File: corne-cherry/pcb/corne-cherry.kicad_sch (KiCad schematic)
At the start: 122 parts, among them J1 MJ-4PP-9, J2 OLED, J3 LED, P1 i2c-pin, P2 i2c-pin, SW1 SW_PUSH, SW10 SW_PUSH, SW11 SW_PUSH, SW12 SW_PUSH, SW13 SW_PUSH, SW14 SW_PUSH, SW15 SW_PUSH, SW16 SW_PUSH, SW17 SW_PUSH, SW18 SW_PUSH, SW19 SW_PUSH, SW2 SW_PUSH, SW20 SW_PUSH, SW21 SW_PUSH, SW22 SW_PUSH, SW23 SW_PUSH, SW24 SW_PUSH, SW25 SW_PUSH, SW26 SW_PUSH, SW3 SW_PUSH, SW4 SW_PUSH, SW5 SW_PUSH, SW6 SW_PUSH, SW7 SW_PUSH, SW8 SW_PUSH, SW9 SW_PUSH, U1 ProMicro, U3 D, U5 D

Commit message: v.1.0
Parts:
- removed H3, H4: MountingHole, EKR82-footprint:HOLE_M3-3.2-3.5, symbol Mechanical:MountingHole
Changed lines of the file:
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@@
-    )
-  )
-  (symbol (lib_id "Mechanical:MountingHole") (at 313.055 66.04 0) (unit 1)
-    (in_bom yes) (on_board yes)
-    (property "Reference" "H3" (id 0) (at 315.595 64.8716 0)
-      (effects (font (size 1.27 1.27)) (justify left))
-    )
-    (property "Value" "MountingHole" (id 1) (at 315.595 67.183 0)
-      (effects (font (size 1.27 1.27)) (justify left))
-    )
-    (property "Footprint" "EKR82-footprint:HOLE_M3-3.2-3.5" (id 2) (at 313.055 66.04 0)
-      (effects (font (size 1.27 1.27)) hide)
-    )
-    (property "Datasheet" "~" (id 3) (at 313.055 66.04 0)
-      (effects (font (size 1.27 1.27)) hide)
-    )
-  )
-  (symbol (lib_id "Mechanical:MountingHole") (at 313.055 70.485 0) (unit 1)
-    (in_bom yes) (on_board yes)
-    (property "Reference" "H4" (id 0) (at 315.595 69.3166 0)
-      (effects (font (size 1.27 1.27)) (justify left))
-    )
-    (property "Value" "MountingHole" (id 1) (at 315.595 71.628 0)
-      (effects (font (size 1.27 1.27)) (justify left))
-    )
-    (property "Footprint" "EKR82-footprint:HOLE_M3-3.2-3.5" (id 2) (at 313.055 70.485 0)
-      (effects (font (size 1.27 1.27)) hide)
-    )
-    (property "Datasheet" "~" (id 3) (at 313.055 70.485 0)
-      (effects (font (size 1.27 1.27)) hide)
     )
   )
@@
       (reference "H2") (unit 1) (value "MountingHole") (footprint "EKR82-footprint:HOLE_M3-3.2-3.5")
     )
-    (path "/00000000-0000-0000-0000-00005d323d8e"
-      (reference "H3") (unit 1) (value "MountingHole") (footprint "EKR82-footprint:HOLE_M3-3.2-3.5")
-    )
-    (path "/00000000-0000-0000-0000-00005d3381c5"
-      (reference "H4") (unit 1) (value "MountingHole") (footprint "EKR82-footprint:HOLE_M3-3.2-3.5")
-    )
     (path "/00000000-0000-0000-0000-00005d34c5d1"

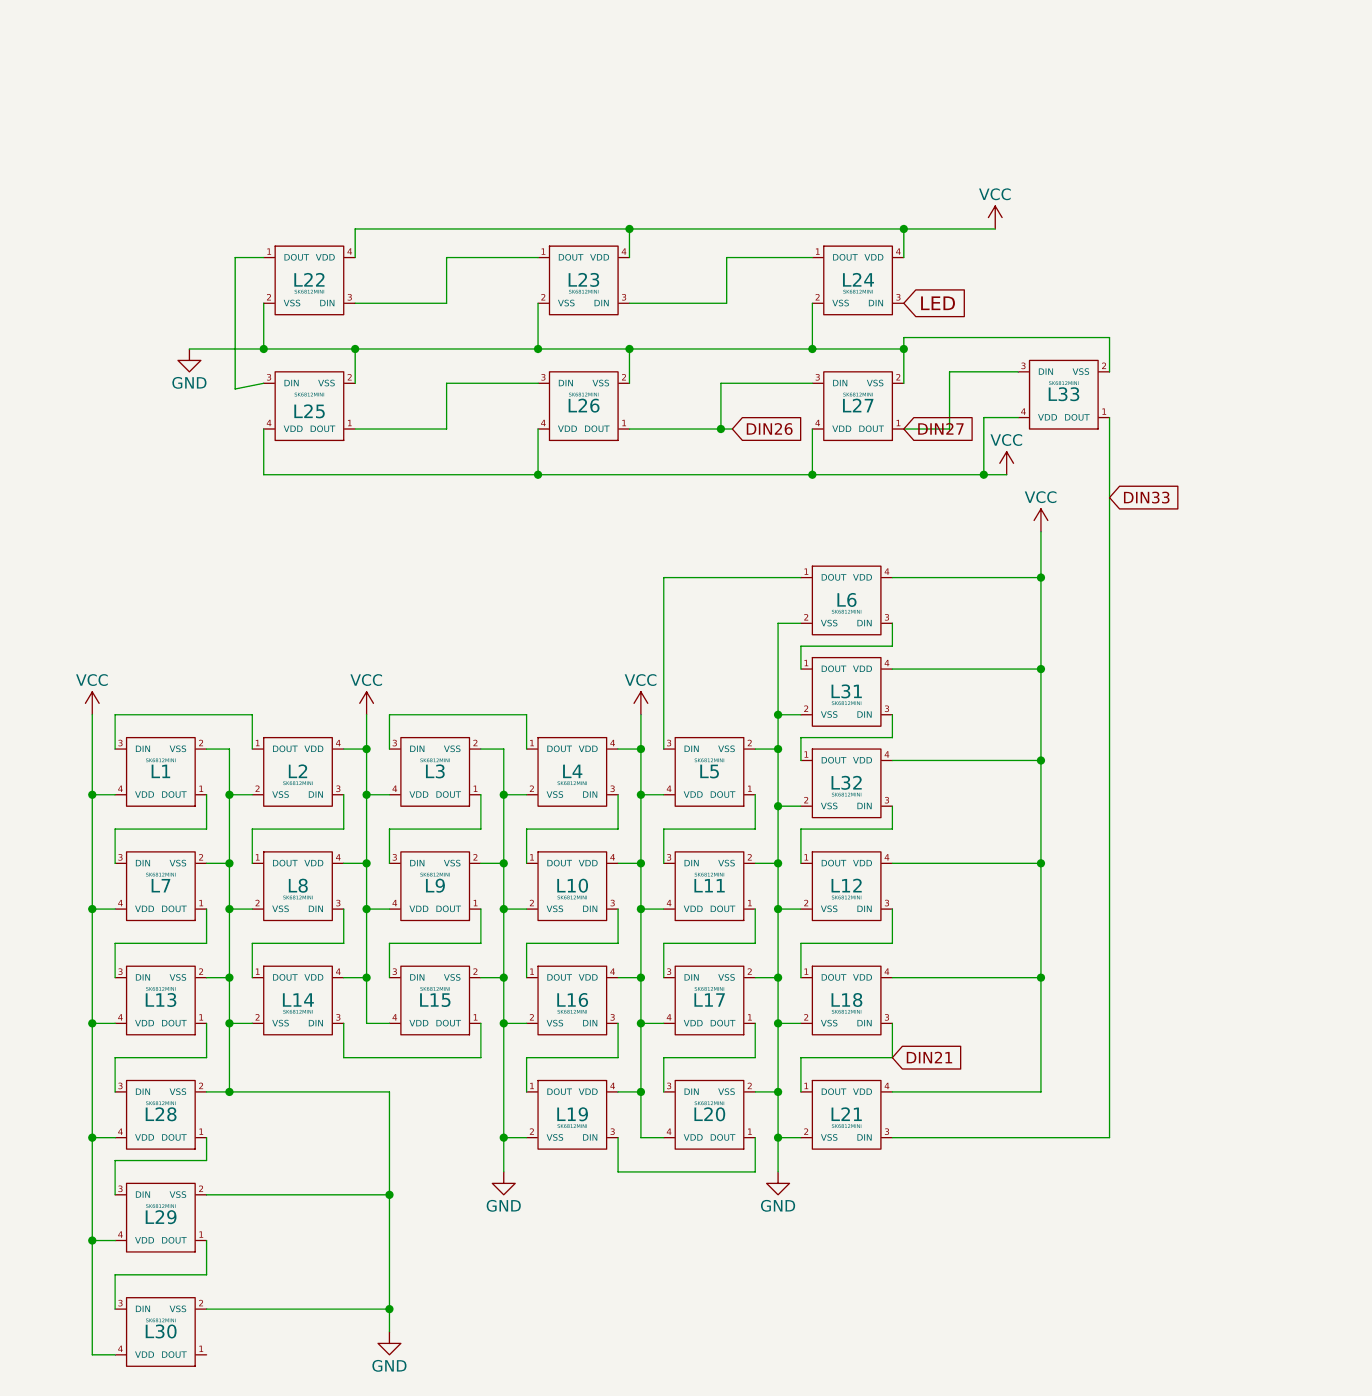
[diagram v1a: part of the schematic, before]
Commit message: Correction Led - new Logo
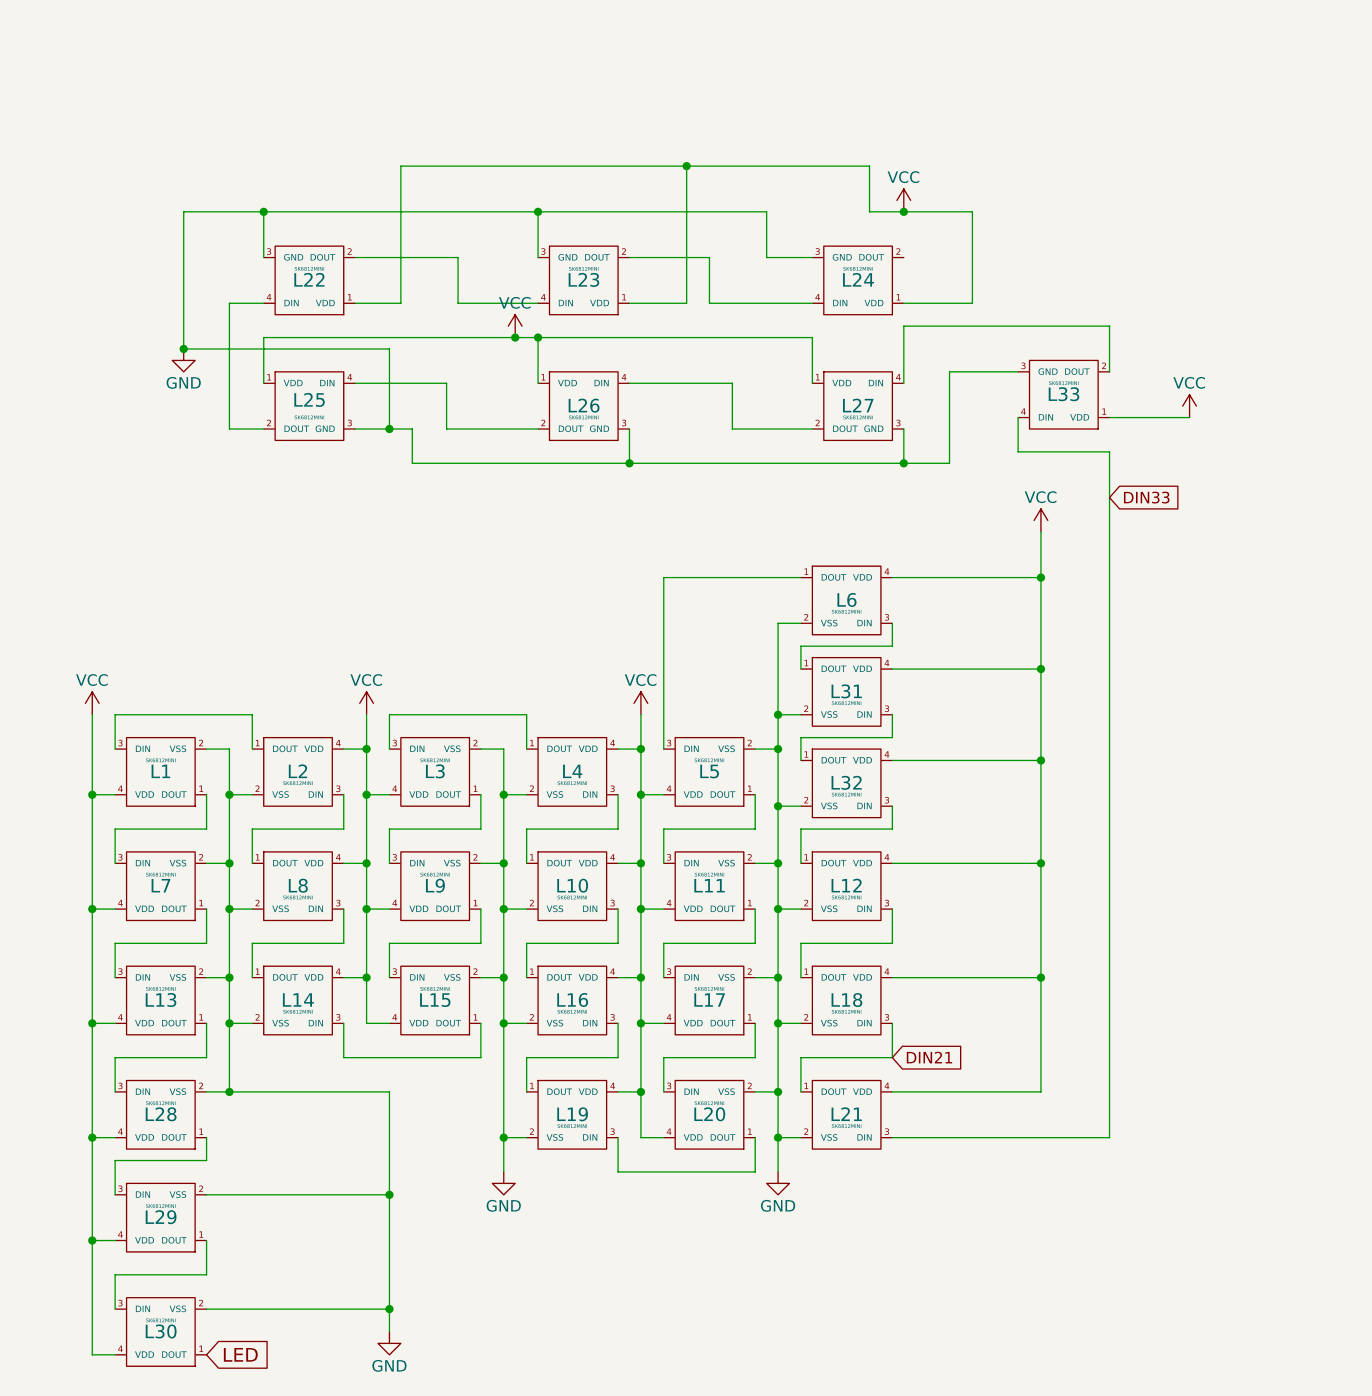
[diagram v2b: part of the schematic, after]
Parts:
- G1, G2: footprint EKR82-footprint:morneLogo F.CU -> EKR82-footprint:RougeGorge
- L24, L25, L26, L27, L33: symbol corne-cherry-rescue:SK6812MINI-kbd-corne-cherry-rescue -> rouge_gorge:SK6812MINI-SMD
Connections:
- net DIN33: now also L33.4 (DIN); no longer L33.1 (DOUT)
- net GND: now also L22.3 (GND), L23.3 (GND), L24.3 (GND), L25.3 (GND), L26.3 (GND), L27.3 (GND), L33.3 (GND); no longer L22.2 (VSS), L23.2 (VSS), L24.2 (VSS), L25.2 (VSS), L26.2 (VSS), L27.2 (VSS), L33.2 (VSS)
- net LED: now also L30.1 (DOUT); no longer L24.3 (DIN)
- net VCC: now also L22.1 (VDD), L23.1 (VDD), L24.1 (VDD), L25.1 (VDD), L26.1 (VDD), L27.1 (VDD), L33.1 (VDD); no longer L22.4 (VDD), L23.4 (VDD), L24.4 (VDD), L25.4 (VDD), L26.4 (VDD), L27.4 (VDD), L33.4 (VDD)
- removed net DIN26: L26.1 (DOUT), L27.3 (DIN)
- removed net DIN27: L27.1 (DOUT), L33.3 (DIN)
- new net: L23.2 (DOUT), L24.4 (DIN)
- new net: L22.2 (DOUT), L23.4 (DIN)
- new net: L22.4 (DIN), L25.2 (DOUT)
- new net: L26.4 (DIN), L27.2 (DOUT)
- new net: L27.4 (DIN), L33.2 (DOUT)
- new net: L25.4 (DIN), L26.2 (DOUT)
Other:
- moved on the sheet: L22, L23, L24, L25, L26, L27
